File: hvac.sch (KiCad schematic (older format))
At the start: 48 parts, among them IC1 ATMEGA328P-A, J1 PROGRAMMING HEADER, J2 SERIAL PORT, J3 POWER_INPUT, SW1 SPST, SW2 SPST, SW3 SPST, U1 MIC5225, U2 MOSFET_N, U3 MOSFET_N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

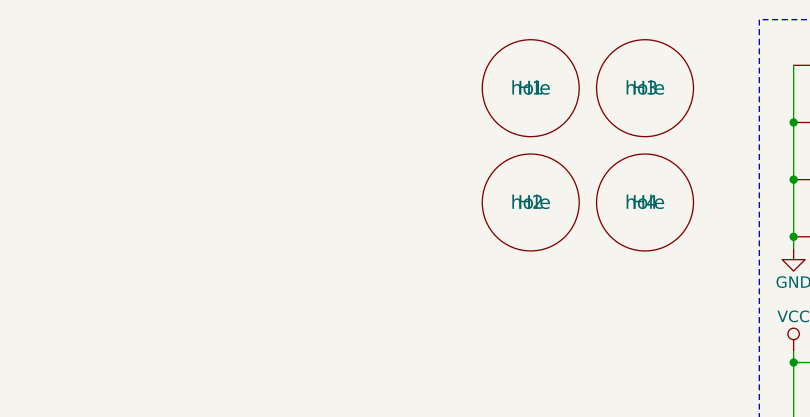
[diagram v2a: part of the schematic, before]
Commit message: Add fiducials to the board for the pick n place
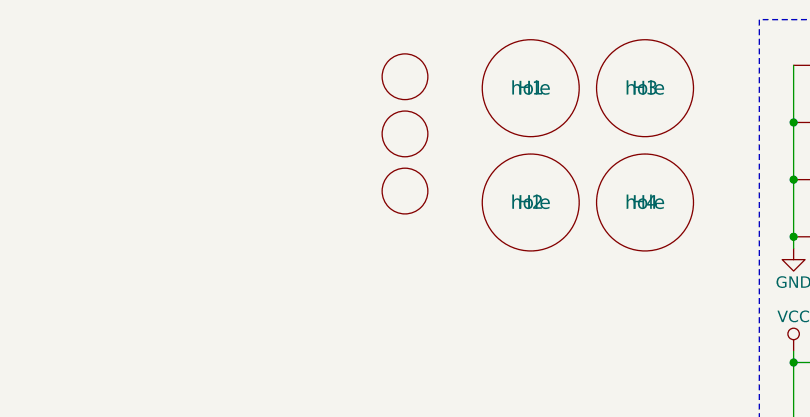
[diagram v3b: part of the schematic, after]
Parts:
- added M1, M2, M3: FIDUCIAL, adafruit:FIDUCIAL_1MM, symbol FIDUCIAL
- H1, H2, H3, H4: footprint (none) -> homebrew:hole-m2.5
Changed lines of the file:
@@
 $EndComp
 $Comp
-L GND #PWR14
+L GND #PWR01
 U 1 1 590E6F18
 P 3900 6550
-F 0 "#PWR14" H 3900 6300 50  0001 C CNN
+F 0 "#PWR01" H 3900 6300 50  0001 C CNN
 F 1 "GND" H 3900 6400 50  0000 C CNN
 F 2 "" H 3900 6550 50  0000 C CNN
@@
 $EndComp
 $Comp
-L GND #PWR17
+L GND #PWR02
 U 1 1 590E705E
 P 4900 6750
-F 0 "#PWR17" H 4900 6500 50  0001 C CNN
+F 0 "#PWR02" H 4900 6500 50  0001 C CNN
 F 1 "GND" H 4900 6600 50  0000 C CNN
 F 2 "" H 4900 6750 50  0000 C CNN
@@
 $EndComp
 $Comp
-L GND #PWR12
+L GND #PWR03
 U 1 1 590E7076
 P 3650 7150
-F 0 "#PWR12" H 3650 6900 50  0001 C CNN
+F 0 "#PWR03" H 3650 6900 50  0001 C CNN
 F 1 "GND" H 3650 7000 50  0000 C CNN
 F 2 "" H 3650 7150 50  0000 C CNN
@@
 $EndComp
 $Comp
-L VCC #PWR15
+L VCC #PWR04
 U 1 1 590E72A3
 P 3900 7600
-F 0 "#PWR15" H 3900 7450 50  0001 C CNN
+F 0 "#PWR04" H 3900 7450 50  0001 C CNN
 F 1 "VCC" H 3900 7750 50  0000 C CNN
 F 2 "" H 3900 7600 50  0000 C CNN
@@
 $EndComp
 $Comp
-L VCC #PWR18
+L VCC #PWR05
 U 1 1 590E73E6
 P 4900 7250
-F 0 "#PWR18" H 4900 7100 50  0001 C CNN
+F 0 "#PWR05" H 4900 7100 50  0001 C CNN
 F 1 "VCC" H 4900 7400 50  0000 C CNN
 F 2 "" H 4900 7250 50  0000 C CNN
@@
 $EndComp
 $Comp
-L +BATT #PWR11
+L +BATT #PWR06
 U 1 1 590E74A1
 P 3600 6950
-F 0 "#PWR11" H 3600 6800 50  0001 C CNN
+F 0 "#PWR06" H 3600 6800 50  0001 C CNN
 F 1 "+BATT" H 3600 7090 50  0000 C CNN
 F 2 "" H 3600 6950 50  0000 C CNN
@@
 $EndComp
 $Comp
-L VCC #PWR6
+L VCC #PWR07
 U 1 1 590E75CA
 P 1200 1500
-F 0 "#PWR6" H 1200 1350 50  0001 C CNN
+F 0 "#PWR07" H 1200 1350 50  0001 C CNN
 F 1 "VCC" H 1200 1650 50  0000 C CNN
 F 2 "" H 1200 1500 50  0000 C CNN
@@
 $EndComp
 $Comp
-L GND #PWR4
+L GND #PWR08
 U 1 1 590E76C4
 P 800 1800
-F 0 "#PWR4" H 800 1550 50  0001 C CNN
+F 0 "#PWR08" H 800 1550 50  0001 C CNN
 F 1 "GND" H 800 1650 50  0000 C CNN
 F 2 "" H 800 1800 50  0000 C CNN
@@
 $EndComp
 $Comp
-L GND #PWR8
+L GND #PWR09
 U 1 1 590E77C7
 P 1850 3600
-F 0 "#PWR8" H 1850 3350 50  0001 C CNN
+F 0 "#PWR09" H 1850 3350 50  0001 C CNN
 F 1 "GND" H 1850 3450 50  0000 C CNN
 F 2 "" H 1850 3600 50  0000 C CNN
@@
 RST
 $Comp
-L GND #PWR5
+L GND #PWR010
 U 1 1 590E81EE
 P 1050 6550
-F 0 "#PWR5" H 1050 6300 50  0001 C CNN
+F 0 "#PWR010" H 1050 6300 50  0001 C CNN
 F 1 "GND" H 1050 6400 50  0000 C CNN
 F 2 "" H 1050 6550 50  0000 C CNN
@@
 TXO
 $Comp
-L VCC #PWR20
+L VCC #PWR011
 U 1 1 590E887E
 P 5500 2650
-F 0 "#PWR20" H 5500 2500 50  0001 C CNN
+F 0 "#PWR011" H 5500 2500 50  0001 C CNN
 F 1 "VCC" H 5500 2800 50  0000 C CNN
 F 2 "" H 5500 2650 50  0000 C CNN
@@
 	4900 6800 4900 6750
 $Comp
-L GND #PWR19
+L GND #PWR012
 U 1 1 590EB74E
 P 5450 7500
-F 0 "#PWR19" H 5450 7250 50  0001 C CNN
+F 0 "#PWR012" H 5450 7250 50  0001 C CNN
 F 1 "GND" H 5450 7350 50  0000 C CNN
 F 2 "" H 5450 7500 50  0000 C CNN
@@
 $EndComp
 $Comp
-L GND #PWR21
+L GND #PWR013
 U 1 1 590EB774
 P 5750 7500
-F 0 "#PWR21" H 5750 7250 50  0001 C CNN
+F 0 "#PWR013" H 5750 7250 50  0001 C CNN
 F 1 "GND" H 5750 7350 50  0000 C CNN
 F 2 "" H 5750 7500 50  0000 C CNN
@@
 $EndComp
 $Comp
-L GND #PWR22
+L GND #PWR014
 U 1 1 590EB798
 P 6050 7500
-F 0 "#PWR22" H 6050 7250 50  0001 C CNN
+F 0 "#PWR014" H 6050 7250 50  0001 C CNN
 F 1 "GND" H 6050 7350 50  0000 C CNN
 F 2 "" H 6050 7500 50  0000 C CNN
@@
 Power Supply
 $Comp
-L GND #PWR23
+L GND #PWR015
 U 1 1 590EC9A4
 P 6350 7500
-F 0 "#PWR23" H 6350 7250 50  0001 C CNN
+F 0 "#PWR015" H 6350 7250 50  0001 C CNN
 F 1 "GND" H 6350 7350 50  0000 C CNN
 F 2 "" H 6350 7500 50  0000 C CNN
@@
 $EndComp
 $Comp
-L GND #PWR28
+L GND #PWR016
 U 1 1 590EF13D
 P 9000 1500
-F 0 "#PWR28" H 9000 1250 50  0001 C CNN
+F 0 "#PWR016" H 9000 1250 50  0001 C CNN
 F 1 "GND" H 9000 1350 50  0000 C CNN
 F 2 "" H 9000 1500 50  0000 C CNN
@@
 $EndComp
 $Comp
-L VCC #PWR29
+L VCC #PWR017
 U 1 1 590EFAF0
 P 9000 1950
-F 0 "#PWR29" H 9000 1800 50  0001 C CNN
+F 0 "#PWR017" H 9000 1800 50  0001 C CNN
 F 1 "VCC" H 9000 2100 50  0000 C CNN
 F 2 "" H 9000 1950 50  0000 C CNN
@@
 	9500 2000 9600 2000
 $Comp
-L GND #PWR33
+L GND #PWR018
 U 1 1 590F0610
 P 10350 2600
-F 0 "#PWR33" H 10350 2350 50  0001 C CNN
+F 0 "#PWR018" H 10350 2350 50  0001 C CNN
 F 1 "GND" H 10350 2450 50  0000 C CNN
 F 2 "" H 10350 2600 50  0000 C CNN
@@
 BTN_TIMER
 $Comp
-L GND #PWR24
+L GND #PWR019
 U 1 1 590F35D5
 P 6650 7500
-F 0 "#PWR24" H 6650 7250 50  0001 C CNN
+F 0 "#PWR019" H 6650 7250 50  0001 C CNN
 F 1 "GND" H 6650 7350 50  0000 C CNN
 F 2 "" H 6650 7500 50  0000 C CNN
@@
 SW_VENT_OVERRIDE
 $Comp
-L GND #PWR2
+L GND #PWR020
 U 1 1 590F5B7A
 P 750 7500
-F 0 "#PWR2" H 750 7250 50  0001 C CNN
+F 0 "#PWR020" H 750 7250 50  0001 C CNN
 F 1 "GND" H 750 7350 50  0000 C CNN
 F 2 "" H 750 7500 50  0000 C CNN
@@
 	750  7500 900  7500
 $Comp
-L VCC #PWR1
+L VCC #PWR021
 U 1 1 590F5CC0
 P 750 7300
-F 0 "#PWR1" H 750 7150 50  0001 C CNN
+F 0 "#PWR021" H 750 7150 50  0001 C CNN
 F 1 "VCC" H 750 7450 50  0000 C CNN
 F 2 "" H 750 7300 50  0000 C CNN
@@
 TEMP_OUTSIDE
 $Comp
-L VCC #PWR30
+L VCC #PWR022
 U 1 1 590F74AC
 P 9150 3200
-F 0 "#PWR30" H 9150 3050 50  0001 C CNN
+F 0 "#PWR022" H 9150 3050 50  0001 C CNN
 F 1 "VCC" H 9150 3350 50  0000 C CNN
 F 2 "" H 9150 3200 50  0000 C CNN
@@
 $EndComp
 $Comp
-L GND #PWR16
+L GND #PWR023
 U 1 1 590FA0A9
 P 4600 6150
-F 0 "#PWR16" H 4600 5900 50  0001 C CNN
+F 0 "#PWR023" H 4600 5900 50  0001 C CNN
 F 1 "GND" H 4600 6000 50  0000 C CNN
 F 2 "" H 4600 6150 50  0000 C CNN
@@
 $EndComp
 $Comp
-L +BATT #PWR13
+L +BATT #PWR024
 U 1 1 590FA14E
 P 3800 6050
-F 0 "#PWR13" H 3800 5900 50  0001 C CNN
+F 0 "#PWR024" H 3800 5900 50  0001 C CNN
 F 1 "+BATT" H 3800 6190 50  0000 C CNN
 F 2 "" H 3800 6050 50  0000 C CNN
@@
 Power Connector
 $Comp
-L GND #PWR10
+L GND #PWR025
 U 1 1 590FBCD1
 P 3100 7550
-F 0 "#PWR10" H 3100 7300 50  0001 C CNN
+F 0 "#PWR025" H 3100 7300 50  0001 C CNN
 F 1 "GND" H 3100 7400 50  0000 C CNN
 F 2 "" H 3100 7550 50  0000 C CNN
@@
 $EndComp
 $Comp
-L +BATT #PWR9
+L +BATT #PWR026
 U 1 1 590FC073
 P 3100 6450
-F 0 "#PWR9" H 3100 6300 50  0001 C CNN
+F 0 "#PWR026" H 3100 6300 50  0001 C CNN
 F 1 "+BATT" H 3100 6590 50  0000 C CNN
 F 2 "" H 3100 6450 50  0000 C CNN
@@
 Programming Ports
 $Comp
-L GND #PWR31
+L GND #PWR027
 U 1 1 590FE215
 P 9250 4200
-F 0 "#PWR31" H 9250 3950 50  0001 C CNN
+F 0 "#PWR027" H 9250 3950 50  0001 C CNN
 F 1 "GND" H 9250 4050 50  0000 C CNN
 F 2 "" H 9250 4200 50  0000 C CNN
@@
 $EndComp
 $Comp
-L GND #PWR26
+L GND #PWR028
 U 1 1 59102A56
 P 8800 5200
-F 0 "#PWR26" H 8800 4950 50  0001 C CNN
+F 0 "#PWR028" H 8800 4950 50  0001 C CNN
 F 1 "GND" H 8800 5050 50  0000 C CNN
 F 2 "" H 8800 5200 50  0000 C CNN
@@
 $EndComp
 $Comp
-L +BATT #PWR32
+L +BATT #PWR029
 U 1 1 59102C3A
 P 9250 4550
-F 0 "#PWR32" H 9250 4400 50  0001 C CNN
+F 0 "#PWR029" H 9250 4400 50  0001 C CNN
 F 1 "+BATT" H 9250 4690 50  0000 C CNN
 F 2 "" H 9250 4550 50  0000 C CNN
@@
 $EndComp
 $Comp
-L GND #PWR27
+L GND #PWR030
 U 1 1 591065E6
 P 8800 6250
-F 0 "#PWR27" H 8800 6000 50  0001 C CNN
+F 0 "#PWR030" H 8800 6000 50  0001 C CNN
 F 1 "GND" H 8800 6100 50  0000 C CNN
 F 2 "" H 8800 6250 50  0000 C CNN
@@
 $EndComp
 $Comp
-L GND #PWR25
+L GND #PWR031
 U 1 1 591067B3
 P 8800 4150
-F 0 "#PWR25" H 8800 3900 50  0001 C CNN
+F 0 "#PWR031" H 8800 3900 50  0001 C CNN
 F 1 "GND" H 8800 4000 50  0000 C CNN
 F 2 "" H 8800 4150 50  0000 C CNN
@@
 $EndComp
 $Comp
-L VCC #PWR3
+L VCC #PWR032
 U 1 1 59112013
 P 800 1150
-F 0 "#PWR3" H 800 1000 50  0001 C CNN
+F 0 "#PWR032" H 800 1000 50  0001 C CNN
 F 1 "VCC" H 800 1300 50  0000 C CNN
 F 2 "" H 800 1150 50  0000 C CNN
@@
 $EndComp
 $Comp
-L GND #PWR7
+L GND #PWR033
 U 1 1 59112187
 P 1200 1800
-F 0 "#PWR7" H 1200 1550 50  0001 C CNN
+F 0 "#PWR033" H 1200 1550 50  0001 C CNN
 F 1 "GND" H 1200 1650 50  0000 C CNN
 F 2 "" H 1200 1800 50  0000 C CNN
@@
 F 0 "H3" H 8350 800 60  0000 C CNN
 F 1 "hole" H 8350 800 60  0000 C CNN
-F 2 "" H 8350 800 60  0000 C CNN
+F 2 "homebrew:hole-m2.5" H 8350 800 60  0001 C CNN
 F 3 "" H 8350 800 60  0000 C CNN
 	1    8350 800
@@
 F 0 "H4" H 8350 1300 60  0000 C CNN
 F 1 "hole" H 8350 1300 60  0000 C CNN
-F 2 "" H 8350 1300 60  0000 C CNN
+F 2 "homebrew:hole-m2.5" H 8350 1300 60  0001 C CNN
 F 3 "" H 8350 1300 60  0000 C CNN
 	1    8350 1300
@@
 F 0 "H1" H 7850 800 60  0000 C CNN
 F 1 "hole" H 7850 800 60  0000 C CNN
-F 2 "" H 7850 800 60  0000 C CNN
+F 2 "homebrew:hole-m2.5" H 7850 800 60  0001 C CNN
 F 3 "" H 7850 800 60  0000 C CNN
 	1    7850 800
@@
 F 0 "H2" H 7850 1300 60  0000 C CNN
 F 1 "hole" H 7850 1300 60  0000 C CNN
-F 2 "" H 7850 1300 60  0000 C CNN
+F 2 "homebrew:hole-m2.5" H 7850 1300 60  0001 C CNN
 F 3 "" H 7850 1300 60  0000 C CNN
 	1    7850 1300
 	1    0    0    -1
 $EndComp
+$Comp
+L FIDUCIAL M1
+U 1 1 5938CF94
+P 7300 750
+F 0 "M1" H 7300 750 50  0001 C CNN
+F 1 "FIDUCIAL" H 7300 750 50  0001 C CNN
+F 2 "adafruit:FIDUCIAL_1MM" H 7330 900 20  0001 C CNN
+F 3 "" H 7300 750 60  0000 C CNN
+	1    7300 750
+	1    0    0    -1
+$EndComp
+$Comp
+L FIDUCIAL M2
+U 1 1 5938D0C2
+P 7300 1000
+F 0 "M2" H 7300 1000 50  0001 C CNN
+F 1 "FIDUCIAL" H 7300 1000 50  0001 C CNN
+F 2 "adafruit:FIDUCIAL_1MM" H 7330 1150 20  0001 C CNN
+F 3 "" H 7300 1000 60  0000 C CNN
+	1    7300 1000
+	1    0    0    -1
+$EndComp
+$Comp
+L FIDUCIAL M3
+U 1 1 5938D134
+P 7300 1250
+F 0 "M3" H 7300 1250 50  0001 C CNN
+F 1 "FIDUCIAL" H 7300 1250 50  0001 C CNN
+F 2 "adafruit:FIDUCIAL_1MM" H 7330 1400 20  0001 C CNN
+F 3 "" H 7300 1250 60  0000 C CNN
+	1    7300 1250
+	1    0    0    -1
+$EndComp

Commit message: Move pieces to fit better
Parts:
- added R? (x2): 4.7k, 0402-RES, symbol RESISTOR0402
- BTN1: footprint homebrew:EG2355-ND -> homebrew:PVA1-OA-H2
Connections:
- net TEMP_INSIDE: now also R?.2
- net TEMP_OUTSIDE: now also R?.2
- net VCC: now also R?.1, R?.1
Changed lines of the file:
@@
 Wire Wire Line
 	3850 2800 4000 2800
-Text GLabel 4000 1800 2    60   Input ~ 0
+Text GLabel 5200 1800 2    60   Input ~ 0
 TEMP_OUTSIDE
-Text GLabel 4000 1900 2    60   Input ~ 0
+Text GLabel 6150 1900 2    60   Input ~ 0
 TEMP_INSIDE
 Wire Wire Line
-	4000 1900 3850 1900
-Wire Wire Line
-	3850 1800 4000 1800
+	3850 1900 6150 1900
+Wire Wire Line
+	3850 1800 5200 1800
 Wire Wire Line
 	3850 2650 5050 2650
@@
 F 0 "BTN1" H 9500 1550 50  0000 C CNN
 F 1 "SPST" H 9500 1350 50  0001 C CNN
-F 2 "homebrew:EG2355-ND" H 9500 1450 50  0001 C CNN
+F 2 "homebrew:PVA1-OA-H2" H 9500 1450 50  0001 C CNN
 F 3 "" H 9500 1450 50  0000 C CNN
 	1    9500 1450
@@
 	1    0    0    -1
 $EndComp
+$Comp
+L RESISTOR0402 R?
+U 1 1 5965B0E5
+P 6050 1650
+F 0 "R?" H 5900 1709 50  0000 L BNN
+F 1 "4.7k" H 5900 1520 50  0000 L BNN
+F 2 "0402-RES" H 6080 1800 20  0001 C CNN
+F 3 "" H 6050 1650 60  0000 C CNN
+	1    6050 1650
+	0    1    1    0
+$EndComp
+$Comp
+L RESISTOR0402 R?
+U 1 1 5965B1A0
+P 5100 1550
+F 0 "R?" H 4950 1609 50  0000 L BNN
+F 1 "4.7k" H 4950 1420 50  0000 L BNN
+F 2 "0402-RES" H 5130 1700 20  0001 C CNN
+F 3 "" H 5100 1550 60  0000 C CNN
+	1    5100 1550
+	0    1    1    0
+$EndComp
+Wire Wire Line
+	5100 1750 5100 1800
+Connection ~ 5100 1800
+Wire Wire Line
+	6050 1900 6050 1850
+Connection ~ 6050 1900
+$Comp
+L VCC #PWR?
+U 1 1 5965C4CF
+P 5100 1350
+F 0 "#PWR?" H 5100 1200 50  0001 C CNN
+F 1 "VCC" H 5100 1500 50  0000 C CNN
+F 2 "" H 5100 1350 50  0000 C CNN
+F 3 "" H 5100 1350 50  0000 C CNN
+	1    5100 1350
+	1    0    0    -1
+$EndComp
+$Comp
+L VCC #PWR?
+U 1 1 5965C60B
+P 6050 1450
+F 0 "#PWR?" H 6050 1300 50  0001 C CNN
+F 1 "VCC" H 6050 1600 50  0000 C CNN
+F 2 "" H 6050 1450 50  0000 C CNN
+F 3 "" H 6050 1450 50  0000 C CNN
+	1    6050 1450
+	1    0    0    -1
+$EndComp

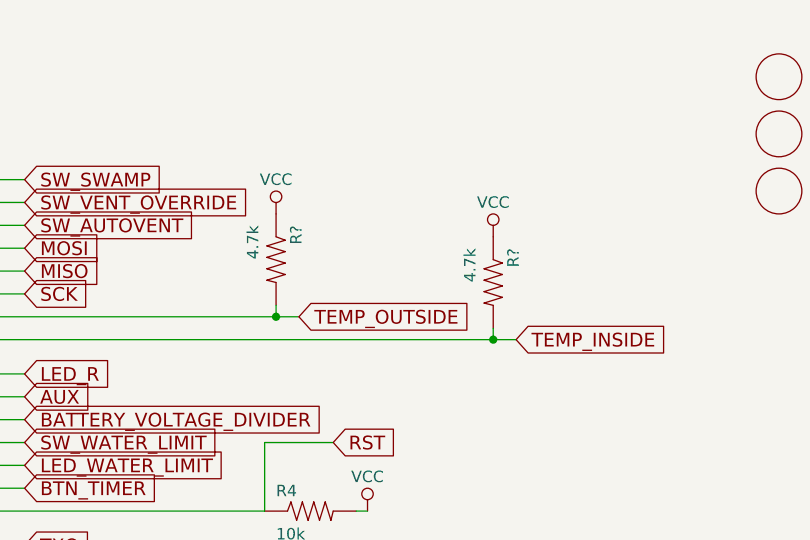
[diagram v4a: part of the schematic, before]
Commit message: Add pullup resistors for temperature probes
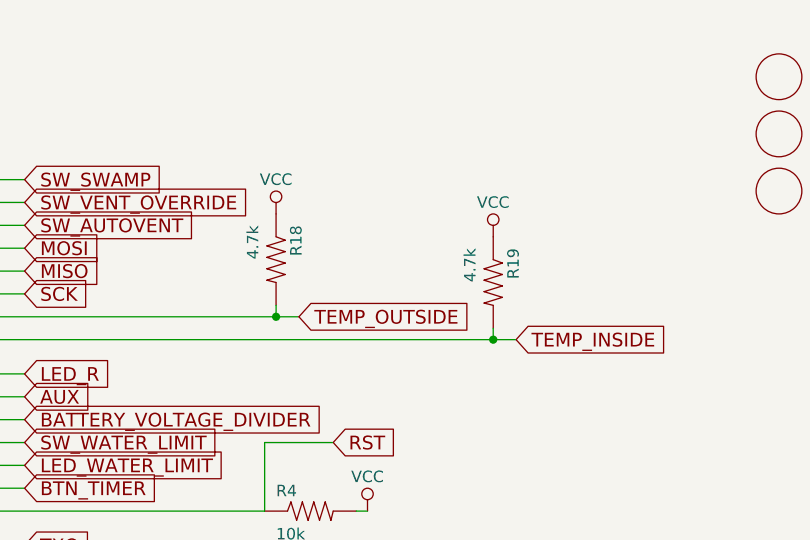
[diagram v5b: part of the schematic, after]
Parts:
- R18, R19: renamed from R?; footprint 0402-RES -> Resistors_SMD:R_0402
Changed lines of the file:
@@
 $EndComp
 $Comp
-L RESISTOR0402 R?
+L RESISTOR0402 R19
 U 1 1 5965B0E5
 P 6050 1650
-F 0 "R?" H 5900 1709 50  0000 L BNN
+F 0 "R19" H 5900 1709 50  0000 L BNN
 F 1 "4.7k" H 5900 1520 50  0000 L BNN
-F 2 "0402-RES" H 6080 1800 20  0001 C CNN
+F 2 "Resistors_SMD:R_0402" H 6080 1800 20  0001 C CNN
 F 3 "" H 6050 1650 60  0000 C CNN
 	1    6050 1650
@@
 $EndComp
 $Comp
-L RESISTOR0402 R?
+L RESISTOR0402 R18
 U 1 1 5965B1A0
 P 5100 1550
-F 0 "R?" H 4950 1609 50  0000 L BNN
+F 0 "R18" H 4950 1609 50  0000 L BNN
 F 1 "4.7k" H 4950 1420 50  0000 L BNN
-F 2 "0402-RES" H 5130 1700 20  0001 C CNN
+F 2 "Resistors_SMD:R_0402" H 5130 1700 20  0001 C CNN
 F 3 "" H 5100 1550 60  0000 C CNN
 	1    5100 1550
@@
 Connection ~ 6050 1900
 $Comp
-L VCC #PWR?
+L VCC #PWR034
 U 1 1 5965C4CF
 P 5100 1350
-F 0 "#PWR?" H 5100 1200 50  0001 C CNN
+F 0 "#PWR034" H 5100 1200 50  0001 C CNN
 F 1 "VCC" H 5100 1500 50  0000 C CNN
 F 2 "" H 5100 1350 50  0000 C CNN
@@
 $EndComp
 $Comp
-L VCC #PWR?
+L VCC #PWR035
 U 1 1 5965C60B
 P 6050 1450
-F 0 "#PWR?" H 6050 1300 50  0001 C CNN
+F 0 "#PWR035" H 6050 1300 50  0001 C CNN
 F 1 "VCC" H 6050 1600 50  0000 C CNN
 F 2 "" H 6050 1450 50  0000 C CNN

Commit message: Bump revision + minor changes
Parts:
- R8: value 2.2k -> 3.3k
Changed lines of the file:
@@
 P 6350 7100
 F 0 "R8" H 6200 7159 50  0000 L BNN
-F 1 "2.2k" H 6200 6970 50  0000 L BNN
+F 1 "3.3k" H 6200 6970 50  0000 L BNN
 F 2 "Resistors_SMD:R_0402" H 6380 7250 20  0001 C CNN
 F 3 "" H 6350 7100 60  0000 C CNN
